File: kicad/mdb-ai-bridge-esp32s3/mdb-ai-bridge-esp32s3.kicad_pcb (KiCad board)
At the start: 2 copper layers, 65 x 40 mm, 94 parts, among them J3 Conn_02x08_Top_Bottom, J7 USB_C_Receptacle_USB2.0_16P, SW3 SW_Push, SW4 SW_Push, SW5 SW_Push, SW6 SW_Push, SW7 SW_Push, SW8 SW_Push, SW9 SW_Push, U10 ESP32-S3FH4R2, U11 ESP32-S3FH4R2, U12 ESP32-S3FH4R2, U13 AMS1117-3.3, U14 USB2514B_Bi, Y2 Crystal_GND24, Y3 Crystal_GND24, Y4 Crystal_GND24, Y5 Crystal_GND24

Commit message: routing...
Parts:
- removed SW6, SW7, SW8: SW_Push, Button_Switch_SMD:SW_Tactile_SPST_NO_Straight_CK_PTS636Sx25SMTRLFS
- added TP1: TestPoint, TestPoint:TestPoint_Pad_D1.5mm, F.Cu at (159.1, 104.3)
- added TP2: TestPoint, TestPoint:TestPoint_Pad_D1.5mm, F.Cu at (139.7, 112.1)
- added TP3: TestPoint, TestPoint:TestPoint_Pad_D1.5mm, F.Cu at (180.1, 105.7)
- C33: value 1.8pf -> 1.8pF
- FB3, FB4, FB5: value FerriteBead_Small -> FerriteBead
- L7: value 2.4nh -> 2.4nH
- R44, R45: value 4K7 -> 4.7k
- Y2: value Crystal_GND24 -> 24MHz
- Y3, Y4, Y5: value Crystal_GND24 -> 40MHz
- moved C10 99.0 mm to (143.2, 77.6), turned to 180 degrees
- moved R2 97.3 mm to (143.2, 79.3), turned to 180 degrees
- moved C2 95.2 mm to (143.3, 81.2), turned to 0 degrees
- moved R3 93.4 mm to (143.3, 83.0), turned to 180 degrees
- moved R10 91.7 mm to (143.3, 84.7), turned to 180 degrees
- moved U14 87.9 mm to (150.0, 82.1), turned to -90 degrees
- moved R11 86.7 mm to (155.2, 79.3), turned to -90 degrees
- moved C8 85.9 mm to (144.0, 90.0), turned to 90 degrees
- moved C3 85.5 mm to (156.8, 79.2), turned to -90 degrees
- moved C20 85.0 mm to (160.4, 77.5), turned to 180 degrees
- moved C9 83.8 mm to (146.0, 90.0), turned to -90 degrees
- moved R9 82.0 mm to (147.8, 89.9), turned to -90 degrees
- moved Y2 81.3 mm to (160.4, 80.5), turned to -90 degrees
- moved R8 80.4 mm to (149.4, 89.9), turned to 90 degrees
- moved R4 79.7 mm to (155.5, 85.2), turned to 90 degrees
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
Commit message: routing...
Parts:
- AE3: footprint RF_Antenna:Texas_SWRA117D_2.4GHz_Left -> RF_Antenna:Texas_SWRA117D_2.4GHz_Right
- moved H2 67.3 mm to (194.4, 83.9)
- moved U13 20.9 mm to (167.9, 83.1), turned to 180 degrees
- moved TP3 18.2 mm to (174.3, 122.9)
- moved TP1 18.2 mm to (153.3, 121.5)
- moved C41 16.0 mm to (167.5, 88.2)
- moved R41 12.3 mm to (174.9, 83.9), turned to -90 degrees
- moved C42 11.7 mm to (171.0, 88.3)
- moved R42 10.7 mm to (175.0, 79.5), turned to -90 degrees
- moved J7 10.2 mm to (181.6, 81.2), turned to 180 degrees
- moved AE3 9.15 mm to (137.2, 111.4)
- moved TP2 8.77 mm to (146.1, 118.1)
- moved C46 4.99 mm to (179.6, 102.8)
- moved FB5 4.99 mm to (177.6, 102.8)
- moved R37 4.99 mm to (177.6, 106.0)
- moved R39 4.99 mm to (181.4, 106.0)
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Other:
- board size 65 x 40 mm -> 63 x 37.9 mm

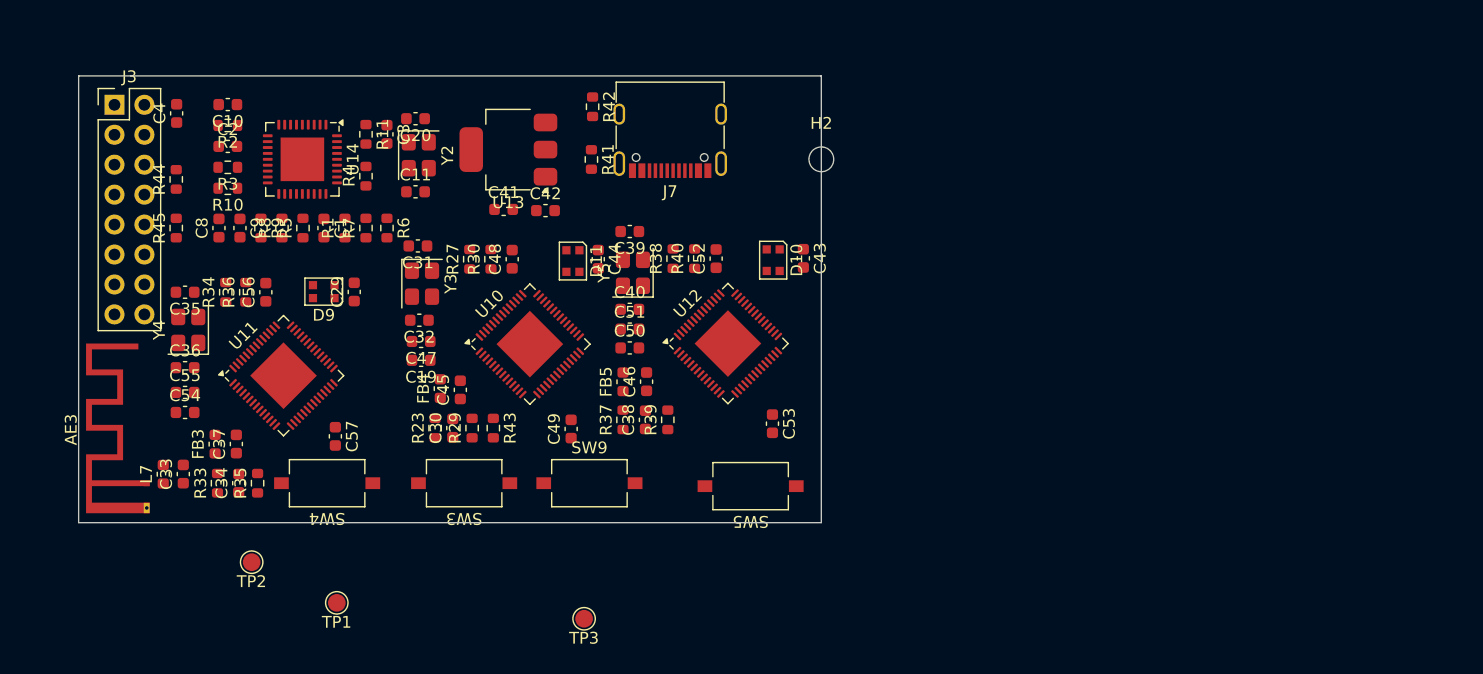
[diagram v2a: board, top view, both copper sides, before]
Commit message: Reorganize PCB layout: declutter, grid-align, rotate R/C, fix labels
- Declutter overlapping/off-board footprints via courtyard-based AABB
  relaxation (241 collisions -> 0, 94 footprints).
- Snap R/C to 0.5mm grid with local collision repair.
- Reflow layout to fit shrunk Edge.Cuts outline.
- Row-align R/C sharing an electrical cluster (17 footprints).
- Rotate 20 R/C 180 deg toward nearest same-net pad for shorter routes.
- Shrink R/C reference labels 1.0mm -> 0.5mm and reposition 50 that
  still collided, per user's chosen option.

Final: 0 courtyard collisions board-wide (only mounting hole H2
intentionally off strict edge margin).
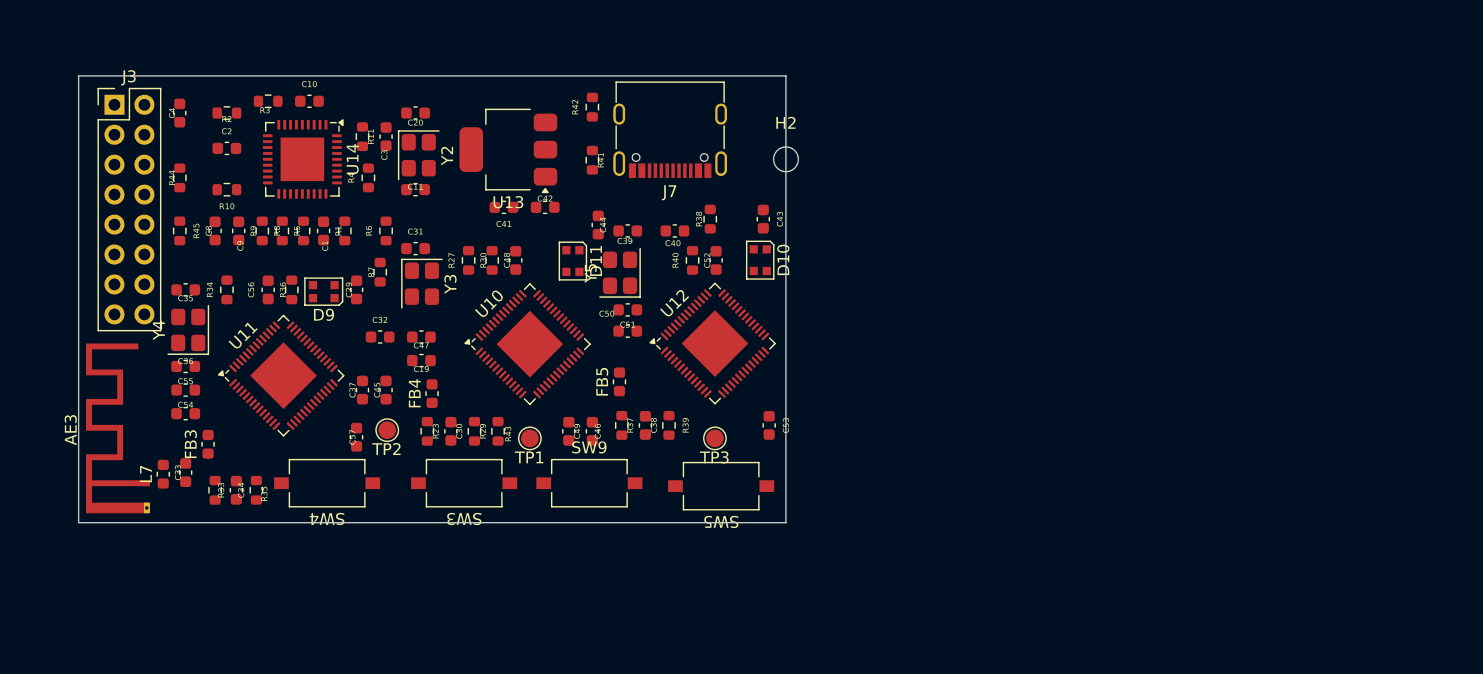
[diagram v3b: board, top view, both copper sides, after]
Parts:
- moved TP1 21.5 mm to (169.7, 107.6)
- moved TP3 18.9 mm to (185.4, 107.6)
- moved TP2 16.1 mm to (157.6, 106.9)
- moved C37 11.6 mm to (155.5, 103.5)
- moved C40 7.67 mm to (182.0, 90.0), turned to 180 degrees
- moved C10 6.93 mm to (151.0, 79.0), turned to 0 degrees
- moved R3 6.57 mm to (147.5, 79.0)
- moved C45 6.30 mm to (157.5, 103.5)
- moved C46 6.24 mm to (175.0, 107.0)
- moved C43 4.76 mm to (189.5, 89.0)
- moved R38 4.60 mm to (185.0, 89.0)
- moved R7 3.93 mm to (157.0, 93.5)
- moved R36 3.91 mm to (149.5, 95.0)
- moved C32 3.62 mm to (157.0, 99.0), turned to 0 degrees
- moved C50 3.23 mm to (178.0, 96.7)
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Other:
- board size 63 x 37.9 mm -> 60 x 37.9 mm
